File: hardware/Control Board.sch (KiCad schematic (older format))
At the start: 42 parts, among them J1 Conn_FTDI, J2 SOLAR, M1 Motor_DC, Q1 IRF7105PbF, Q2 BC817W, Q3 BC817W, Q4 IRF7105PbF, SW1 SW_Push, SW2 SW_Push, SW3 SW_Push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

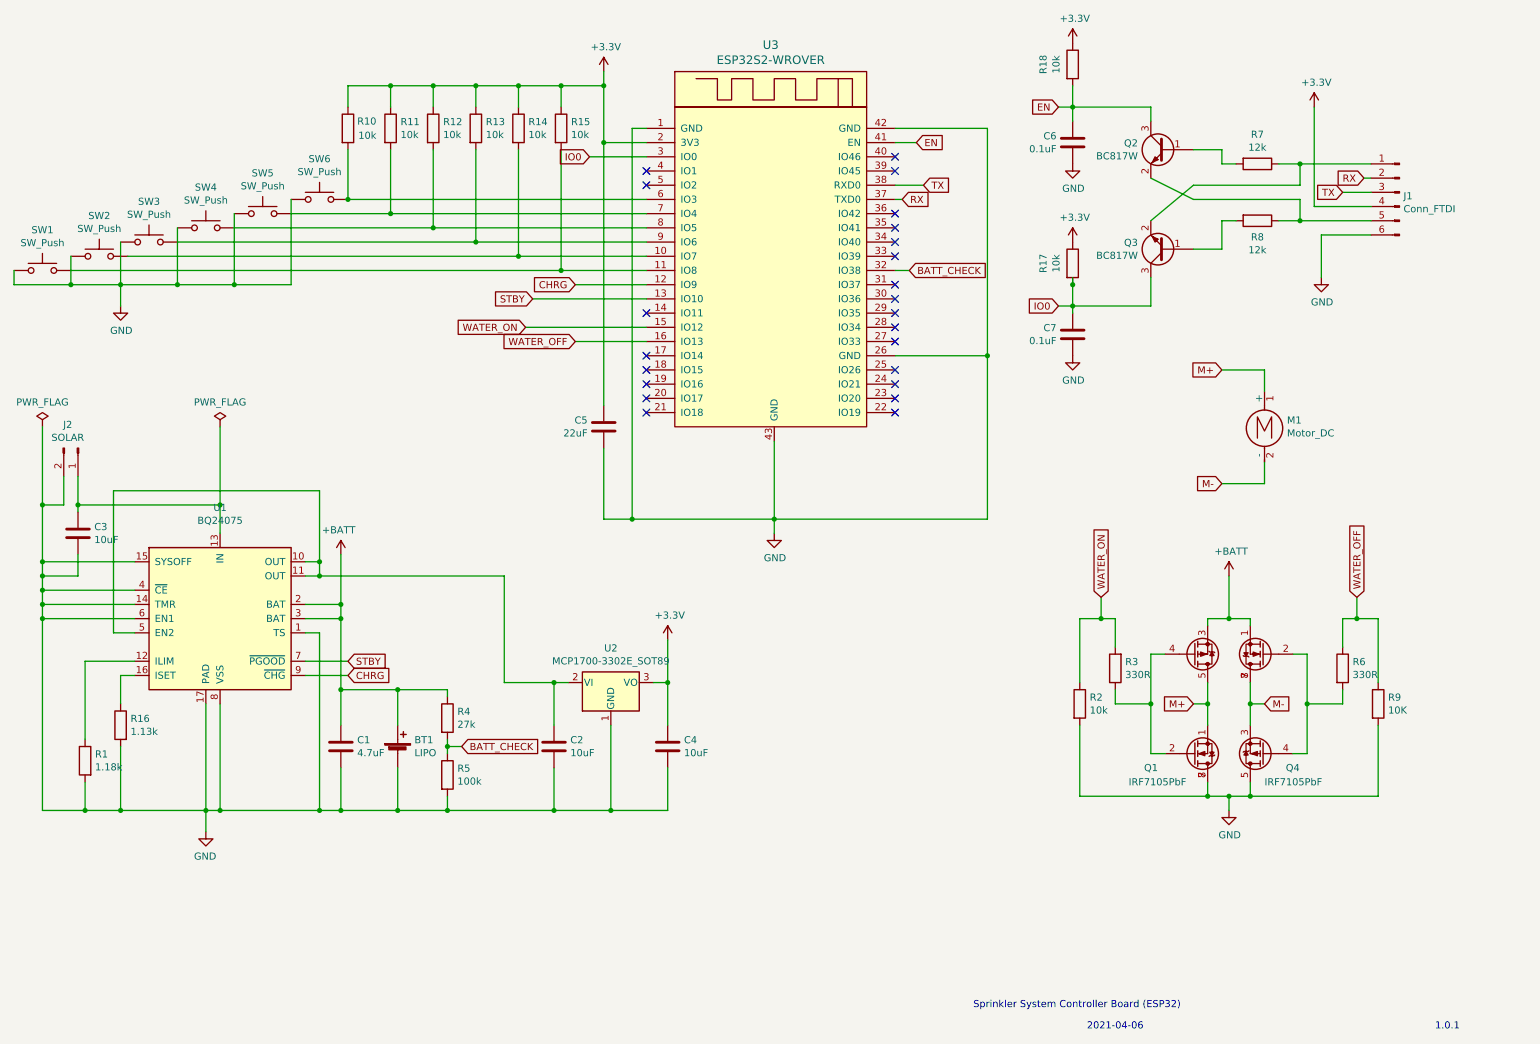
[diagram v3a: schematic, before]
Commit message: Using 5V FTDI, adding protection diodes to allow dual power, adding some additional bypass caps
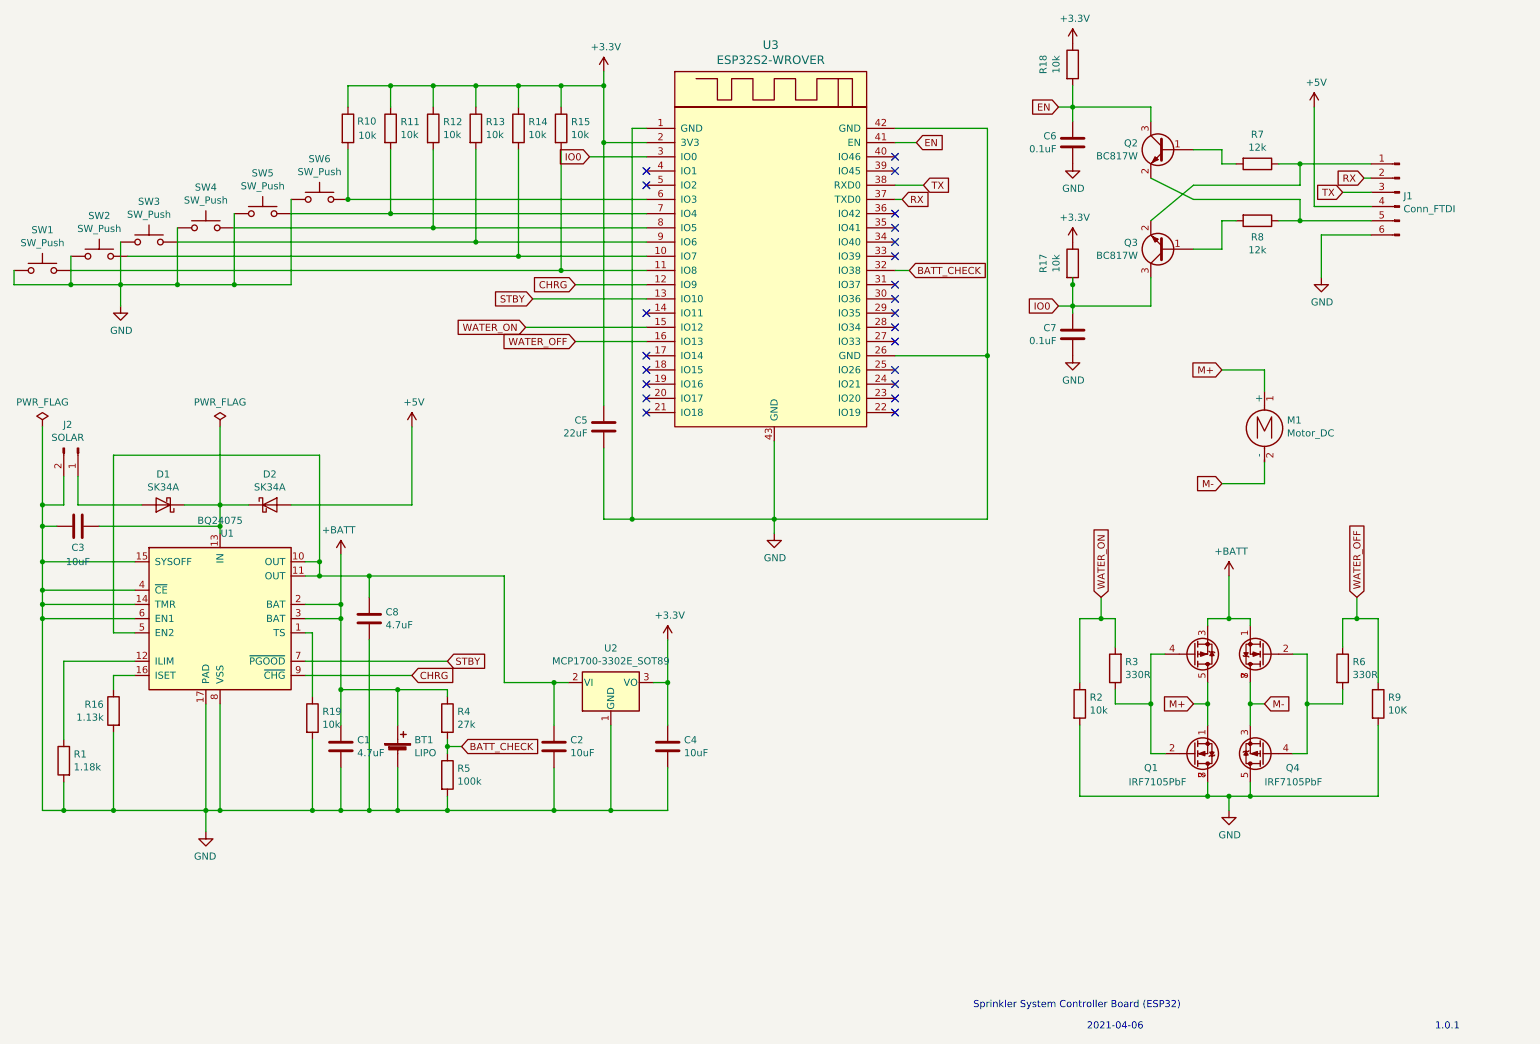
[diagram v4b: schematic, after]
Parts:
- added C8: 4.7uF, Capacitor_SMD:C_0805_2012Metric, symbol Device:C
- added D1, D2: SK34A, Diode_SMD:D_SMA, symbol Device:D_Schottky
- added R19: 10k, Resistor_SMD:R_0805_2012Metric, symbol Device:R
- C1, C2, C3, C4, C5, C6, C7: footprint Capacitor_SMD:C_0402_1005Metric -> Capacitor_SMD:C_0805_2012Metric
- R1, R10, R11, R12, R13, R14, R15, R16, R17, R18, R2, R3, R4, R5, R6, R7, R8, R9: footprint Resistor_SMD:R_0402_1005Metric -> Resistor_SMD:R_0805_2012Metric
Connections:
- net +3V3: no longer J1.4 (Pin_4)
- net GND: now also C3.1, C8.2, R19.2; no longer C3.2, U1.1 (TS)
- net at C2.1, U1.10 (OUT), U1.11 (OUT)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: now also C8.1
- new net: D1.2 (A), J2.1 (Pin_1)
- new net: R19.1, U1.1 (TS)
- new net: C3.2, D1.1 (K), D2.1 (K), U1.13 (IN)
- new net +5V: D2.2 (A), J1.4 (Pin_4)
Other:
- moved on the sheet: C3, R1, R16

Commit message: Using 5V FTDI, adding protection diodes to allow dual power, adding some additional bypass caps
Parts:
- C1, C2, C3, C4, C5, C6, C7, C8: footprint Capacitor_SMD:C_0805_2012Metric -> Capacitor_SMD:C_0402_1005Metric
- R1, R10, R11, R12, R13, R14, R15, R16, R17, R18, R19, R2, R3, R4, R5, R6, R7, R8, R9: footprint Resistor_SMD:R_0805_2012Metric -> Resistor_SMD:R_0402_1005Metric
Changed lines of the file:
@@
 F 0 "R7" V 9143 1550 50  0000 C CNN
 F 1 "12k" V 9234 1550 50  0000 C CNN
-F 2 "Resistor_SMD:R_0805_2012Metric" V 9280 1550 50  0001 C CNN
+F 2 "Resistor_SMD:R_0402_1005Metric" V 9280 1550 50  0001 C CNN
 F 3 "~" H 9350 1550 50  0001 C CNN
 	1    9350 1550
@@
 F 0 "R8" V 9465 1950 50  0000 C CNN
 F 1 "12k" V 9556 1950 50  0000 C CNN
-F 2 "Resistor_SMD:R_0805_2012Metric" V 9280 1950 50  0001 C CNN
+F 2 "Resistor_SMD:R_0402_1005Metric" V 9280 1950 50  0001 C CNN
 F 3 "~" H 9350 1950 50  0001 C CNN
 	1    9350 1950
@@
 F 0 "C1" H 3015 5696 50  0000 L CNN
 F 1 "4.7uF" H 3015 5605 50  0000 L CNN
-F 2 "Capacitor_SMD:C_0805_2012Metric" H 2938 5500 50  0001 C CNN
+F 2 "Capacitor_SMD:C_0402_1005Metric" H 2938 5500 50  0001 C CNN
 F 3 "~" H 2900 5650 50  0001 C CNN
 	1    2900 5650
@@
 F 0 "C4" H 5315 5696 50  0000 L CNN
 F 1 "10uF" H 5315 5605 50  0000 L CNN
-F 2 "Capacitor_SMD:C_0805_2012Metric" H 5238 5500 50  0001 C CNN
+F 2 "Capacitor_SMD:C_0402_1005Metric" H 5238 5500 50  0001 C CNN
 F 3 "~" H 5200 5650 50  0001 C CNN
 	1    5200 5650
@@
 F 0 "C2" H 4515 5696 50  0000 L CNN
 F 1 "10uF" H 4515 5605 50  0000 L CNN
-F 2 "Capacitor_SMD:C_0805_2012Metric" H 4438 5500 50  0001 C CNN
+F 2 "Capacitor_SMD:C_0402_1005Metric" H 4438 5500 50  0001 C CNN
 F 3 "~" H 4400 5650 50  0001 C CNN
 	1    4400 5650
@@
 F 0 "R3" H 8280 5054 50  0000 R CNN
 F 1 "330R" H 8280 5145 50  0000 R CNN
-F 2 "Resistor_SMD:R_0805_2012Metric" V 8280 5100 50  0001 C CNN
+F 2 "Resistor_SMD:R_0402_1005Metric" V 8280 5100 50  0001 C CNN
 F 3 "~" H 8350 5100 50  0001 C CNN
 	1    8350 5100
@@
 F 0 "R6" H 10020 5146 50  0000 L CNN
 F 1 "330R" H 10020 5055 50  0000 L CNN
-F 2 "Resistor_SMD:R_0805_2012Metric" V 9880 5100 50  0001 C CNN
+F 2 "Resistor_SMD:R_0402_1005Metric" V 9880 5100 50  0001 C CNN
 F 3 "~" H 9950 5100 50  0001 C CNN
 	1    9950 5100
@@
 F 0 "R2" H 8170 5396 50  0000 L CNN
 F 1 "10k" H 8170 5305 50  0000 L CNN
-F 2 "Resistor_SMD:R_0805_2012Metric" V 8030 5350 50  0001 C CNN
+F 2 "Resistor_SMD:R_0402_1005Metric" V 8030 5350 50  0001 C CNN
 F 3 "~" H 8100 5350 50  0001 C CNN
 	1    8100 5350
@@
 F 0 "R9" H 10270 5396 50  0000 L CNN
 F 1 "10K" H 10270 5305 50  0000 L CNN
-F 2 "Resistor_SMD:R_0805_2012Metric" V 10130 5350 50  0001 C CNN
+F 2 "Resistor_SMD:R_0402_1005Metric" V 10130 5350 50  0001 C CNN
 F 3 "~" H 10200 5350 50  0001 C CNN
 	1    10200 5350
@@
 F 0 "C5" H 4636 3446 50  0000 R CNN
 F 1 "22uF" H 4636 3355 50  0000 R CNN
-F 2 "Capacitor_SMD:C_0805_2012Metric" H 4788 3250 50  0001 C CNN
+F 2 "Capacitor_SMD:C_0402_1005Metric" H 4788 3250 50  0001 C CNN
 F 3 "~" H 4750 3400 50  0001 C CNN
 	1    4750 3400
@@
 F 0 "R15" H 4520 1346 50  0000 L CNN
 F 1 "10k" H 4520 1255 50  0000 L CNN
-F 2 "Resistor_SMD:R_0805_2012Metric" V 4380 1300 50  0001 C CNN
+F 2 "Resistor_SMD:R_0402_1005Metric" V 4380 1300 50  0001 C CNN
 F 3 "~" H 4450 1300 50  0001 C CNN
 	1    4450 1300
@@
 F 0 "R14" H 4220 1346 50  0000 L CNN
 F 1 "10k" H 4220 1255 50  0000 L CNN
-F 2 "Resistor_SMD:R_0805_2012Metric" V 4080 1300 50  0001 C CNN
+F 2 "Resistor_SMD:R_0402_1005Metric" V 4080 1300 50  0001 C CNN
 F 3 "~" H 4150 1300 50  0001 C CNN
 	1    4150 1300
@@
 F 0 "R13" H 3920 1346 50  0000 L CNN
 F 1 "10k" H 3920 1255 50  0000 L CNN
-F 2 "Resistor_SMD:R_0805_2012Metric" V 3780 1300 50  0001 C CNN
+F 2 "Resistor_SMD:R_0402_1005Metric" V 3780 1300 50  0001 C CNN
 F 3 "~" H 3850 1300 50  0001 C CNN
 	1    3850 1300
@@
 F 0 "R12" H 3620 1346 50  0000 L CNN
 F 1 "10k" H 3620 1255 50  0000 L CNN
-F 2 "Resistor_SMD:R_0805_2012Metric" V 3480 1300 50  0001 C CNN
+F 2 "Resistor_SMD:R_0402_1005Metric" V 3480 1300 50  0001 C CNN
 F 3 "~" H 3550 1300 50  0001 C CNN
 	1    3550 1300
@@
 F 0 "R11" H 3320 1346 50  0000 L CNN
 F 1 "10k" H 3320 1255 50  0000 L CNN
-F 2 "Resistor_SMD:R_0805_2012Metric" V 3180 1300 50  0001 C CNN
+F 2 "Resistor_SMD:R_0402_1005Metric" V 3180 1300 50  0001 C CNN
 F 3 "~" H 3250 1300 50  0001 C CNN
 	1    3250 1300
@@
 F 0 "R10" H 3150 1350 50  0000 R CNN
 F 1 "10k" H 3150 1250 50  0000 R CNN
-F 2 "Resistor_SMD:R_0805_2012Metric" V 2880 1300 50  0001 C CNN
+F 2 "Resistor_SMD:R_0402_1005Metric" V 2880 1300 50  0001 C CNN
 F 3 "~" H 2950 1300 50  0001 C CNN
 	1    2950 1300
@@
 F 0 "R5" H 3720 5896 50  0000 L CNN
 F 1 "100k" H 3720 5805 50  0000 L CNN
-F 2 "Resistor_SMD:R_0805_2012Metric" V 3580 5850 50  0001 C CNN
+F 2 "Resistor_SMD:R_0402_1005Metric" V 3580 5850 50  0001 C CNN
 F 3 "~" H 3650 5850 50  0001 C CNN
 	1    3650 5850
@@
 F 0 "R4" H 3720 5496 50  0000 L CNN
 F 1 "27k" H 3720 5405 50  0000 L CNN
-F 2 "Resistor_SMD:R_0805_2012Metric" V 3580 5450 50  0001 C CNN
+F 2 "Resistor_SMD:R_0402_1005Metric" V 3580 5450 50  0001 C CNN
 F 3 "~" H 3650 5450 50  0001 C CNN
 	1    3650 5450
@@
 F 0 "R16" H 1369 5446 50  0000 L CNN
 F 1 "1.13k" H 1369 5355 50  0000 L CNN
-F 2 "Resistor_SMD:R_0805_2012Metric" V 1230 5400 50  0001 C CNN
+F 2 "Resistor_SMD:R_0402_1005Metric" V 1230 5400 50  0001 C CNN
 F 3 "~" H 1300 5400 50  0001 C CNN
 	1    1300 5400
@@
 F 0 "R1" H 880 5796 50  0000 R CNN
 F 1 "1.18k" H 880 5705 50  0000 R CNN
-F 2 "Resistor_SMD:R_0805_2012Metric" V 880 5750 50  0001 C CNN
+F 2 "Resistor_SMD:R_0402_1005Metric" V 880 5750 50  0001 C CNN
 F 3 "~" H 950 5750 50  0001 C CNN
 	1    950  5750
@@
 F 0 "C3" V 900 4100 50  0000 C CNN
 F 1 "10uF" V 800 4100 50  0000 C CNN
-F 2 "Capacitor_SMD:C_0805_2012Metric" H 1088 3950 50  0001 C CNN
+F 2 "Capacitor_SMD:C_0402_1005Metric" H 1088 3950 50  0001 C CNN
 F 3 "~" H 1050 4100 50  0001 C CNN
 	1    1050 4100
@@
 F 0 "R18" V 7843 850 50  0000 C CNN
 F 1 "10k" V 7934 850 50  0000 C CNN
-F 2 "Resistor_SMD:R_0805_2012Metric" V 7980 850 50  0001 C CNN
+F 2 "Resistor_SMD:R_0402_1005Metric" V 7980 850 50  0001 C CNN
 F 3 "~" H 8050 850 50  0001 C CNN
 	1    8050 850
@@
 F 0 "R17" V 7843 2250 50  0000 C CNN
 F 1 "10k" V 7934 2250 50  0000 C CNN
-F 2 "Resistor_SMD:R_0805_2012Metric" V 7980 2250 50  0001 C CNN
+F 2 "Resistor_SMD:R_0402_1005Metric" V 7980 2250 50  0001 C CNN
 F 3 "~" H 8050 2250 50  0001 C CNN
 	1    8050 2250
@@
 F 0 "C7" H 7936 2796 50  0000 R CNN
 F 1 "0.1uF" H 7936 2705 50  0000 R CNN
-F 2 "Capacitor_SMD:C_0805_2012Metric" H 8088 2600 50  0001 C CNN
+F 2 "Capacitor_SMD:C_0402_1005Metric" H 8088 2600 50  0001 C CNN
 F 3 "~" H 8050 2750 50  0001 C CNN
 	1    8050 2750
@@
 F 0 "C6" H 7936 1446 50  0000 R CNN
 F 1 "0.1uF" H 7936 1355 50  0000 R CNN
-F 2 "Capacitor_SMD:C_0805_2012Metric" H 8088 1250 50  0001 C CNN
+F 2 "Capacitor_SMD:C_0402_1005Metric" H 8088 1250 50  0001 C CNN
 F 3 "~" H 8050 1400 50  0001 C CNN
 	1    8050 1400
@@
 F 0 "R19" H 2770 5496 50  0000 L CNN
 F 1 "10k" H 2770 5405 50  0000 L CNN
-F 2 "Resistor_SMD:R_0805_2012Metric" V 2630 5450 50  0001 C CNN
+F 2 "Resistor_SMD:R_0402_1005Metric" V 2630 5450 50  0001 C CNN
 F 3 "~" H 2700 5450 50  0001 C CNN
 	1    2700 5450
@@
 F 0 "C8" H 3215 4796 50  0000 L CNN
 F 1 "4.7uF" H 3215 4705 50  0000 L CNN
-F 2 "Capacitor_SMD:C_0805_2012Metric" H 3138 4600 50  0001 C CNN
+F 2 "Capacitor_SMD:C_0402_1005Metric" H 3138 4600 50  0001 C CNN
 F 3 "~" H 3100 4750 50  0001 C CNN
 	1    3100 4750

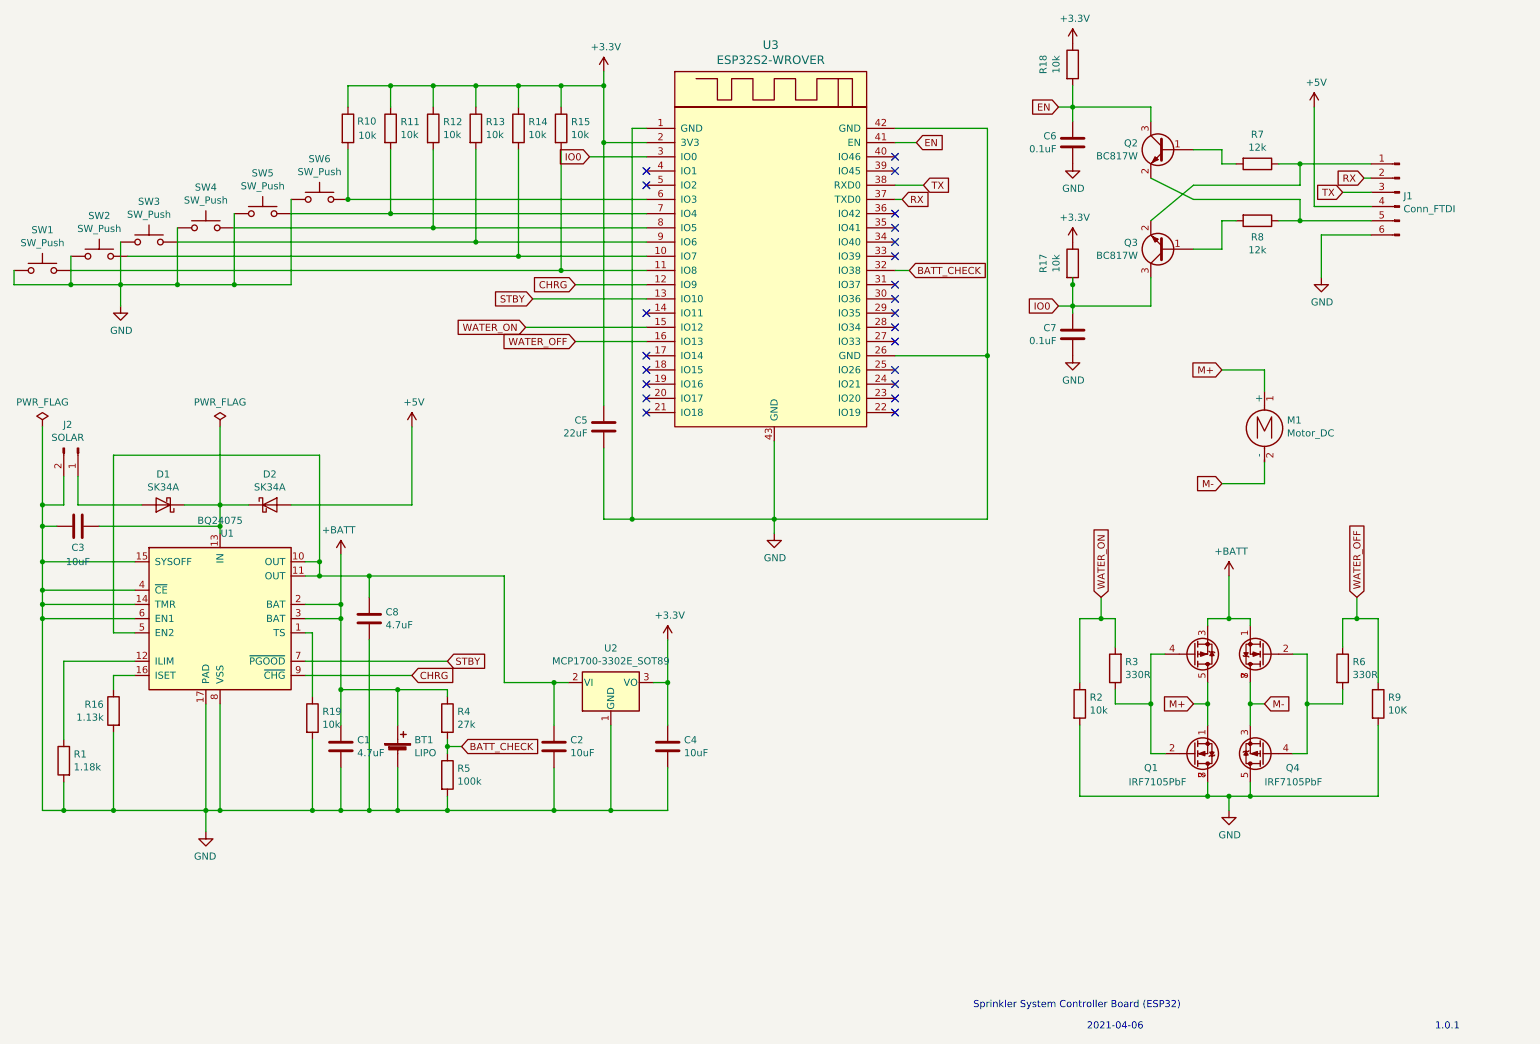
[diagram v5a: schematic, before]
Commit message: Copying board from firmware/powered
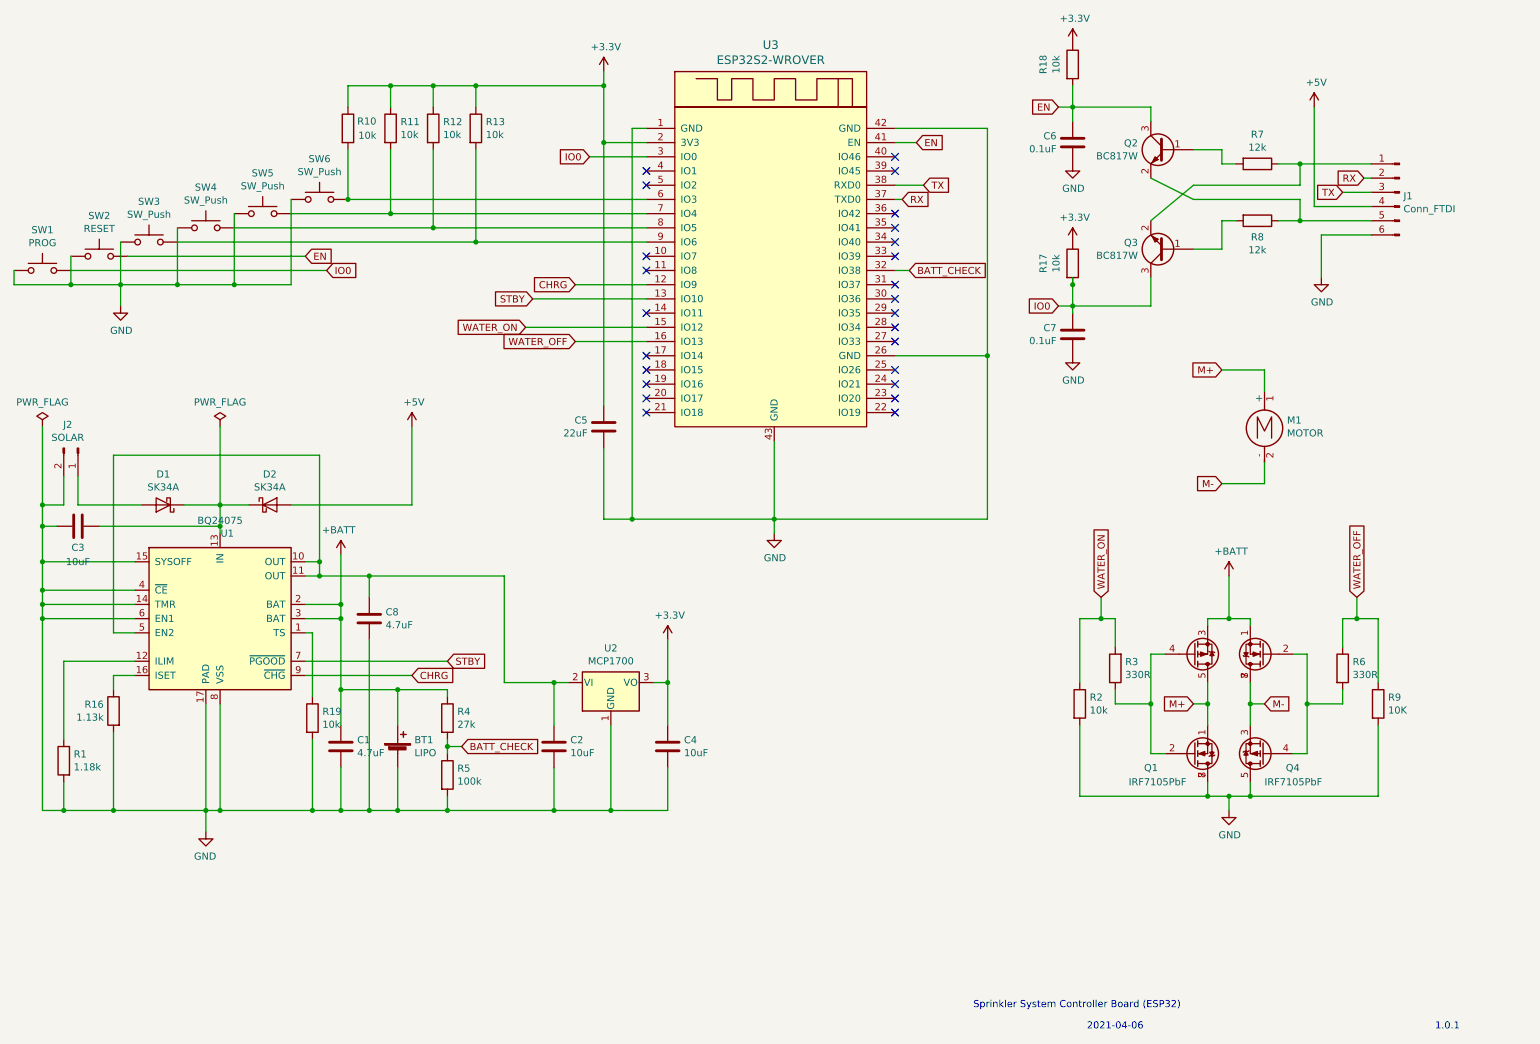
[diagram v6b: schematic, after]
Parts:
- removed R14, R15: 10k, Resistor_SMD:R_0402_1005Metric, symbol Device:R
- M1: value Motor_DC -> MOTOR
- SW1: value SW_Push -> PROG
- SW2: value SW_Push -> RESET
- U1: footprint Package_DFN_QFN:Texas_S-PVQFN-N16_EP2.7x2.7mm -> Package_DFN_QFN:Texas_S-PVQFN-N16_EP2.7x2.7mm_ThermalVias
- U2: value MCP1700-3302E_SOT89 -> MCP1700
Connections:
- net EN: now also SW2.2
- net IO0: now also SW1.2
- net at U3.11 (IO8): no longer SW1.2
- net at U3.10 (IO7): no longer SW2.2
- no-connect marks 23 -> 25
